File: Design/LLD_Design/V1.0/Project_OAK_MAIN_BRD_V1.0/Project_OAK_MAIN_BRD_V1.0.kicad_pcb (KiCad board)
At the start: 4 copper layers, 41.8 x 46 mm, 114 parts, among them U1 ATmega328PB-MU, U2 RV-8263-C7-32.768KHZ-20PPM-TA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, U3 BMA400, U4 DRV2605LYZF

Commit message: Final files prior to DFM check
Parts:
- added G***: LOGO, AI_logo:Project_OAK_V1.0_logo, F.Cu at (73.1, 99.6)
- added G***: LOGO, AI_logo:Project_OAK_V1.0_logo, F.Cu at (70.9, 100.0)
- added G***: LOGO, AI_logo:AI_logo_v1, F.Cu at (70.5, 90.8)
- moved TP7 3.82 mm to (71.7, 96.1)
- moved TP6 2.93 mm to (69.2, 96.1)
- moved TP11 2.73 mm to (67.3, 92.1)
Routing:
- net /PB7: track 4.90 -> 2.03 mm
- net /PB6: track 2.23 -> 4.99 mm
- net /LGT_ON_BTN: track 25.0 -> 27.5 mm
- net /PE1: track 25.2 -> 26.7 mm
- net /UP_BTN: track 27.3 -> 28.7 mm
- net /SNS_SCL: track 27.4 -> 28.4 mm
- net /RTC_CLKO: track 3.71 -> 4.53 mm
- net GND: track 76.8 -> 76.2 mm, vias 75 -> 74
- net /PE2: track 17.9 -> 17.7 mm, vias 2 -> 3

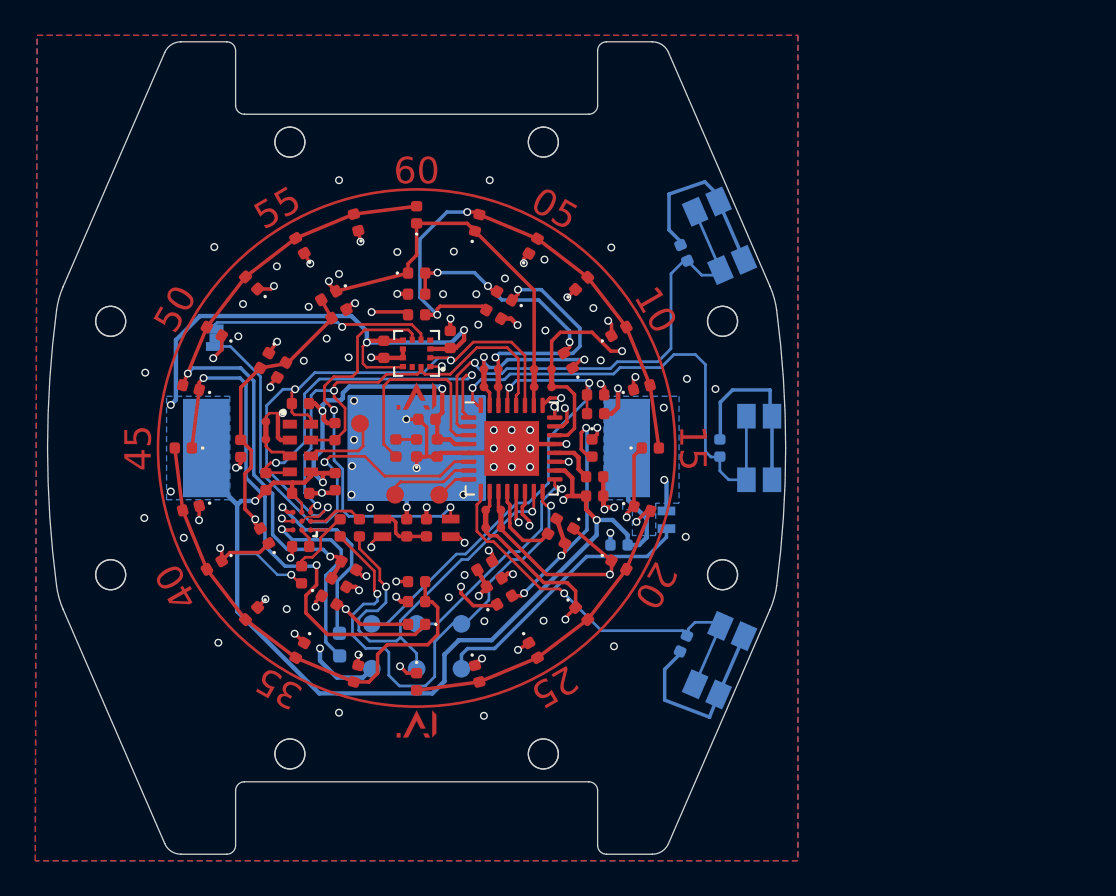
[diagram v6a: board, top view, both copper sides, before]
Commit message: updated PCB based on JLCPCB DFM comments and generated final files
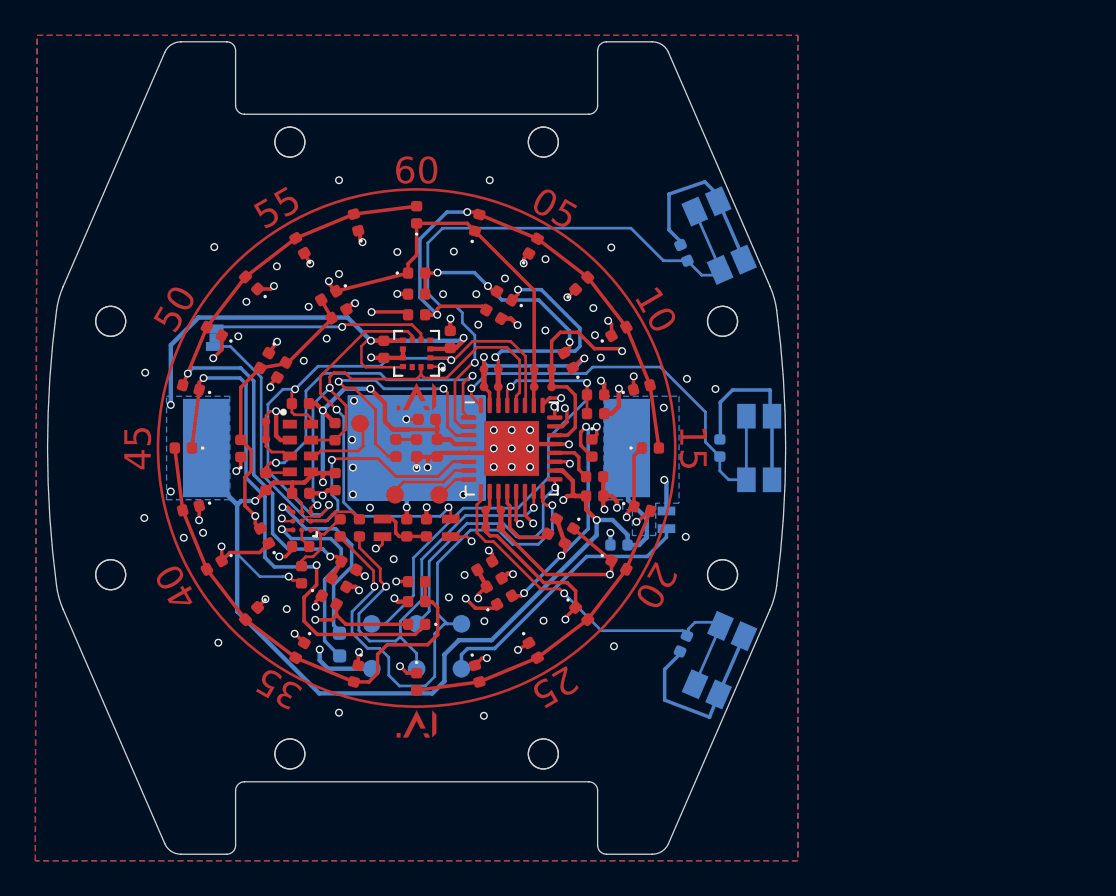
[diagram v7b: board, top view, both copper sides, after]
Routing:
- net /UP_BTN: track 28.7 -> 35.4 mm
- net /MON_LED: track 12.1 -> 15.9 mm, vias 0 -> 2
- net /ICSP_MISO: track 28.5 -> 32.0 mm
- net +3V0: track 137.8 -> 134.8 mm
- net /LGT_ON_BTN: track 27.5 -> 25.0 mm
- net /ICSP_SCK: track 13.2 -> 14.8 mm
- net GND: track 76.2 -> 74.9 mm, vias 74 -> 77
- net /ACC_INT2: track 22.4 -> 21.5 mm
- net /R5: track 88.9 -> 89.8 mm
- net /R2: track 65.9 -> 66.8 mm
- net /ICSP_MOSI: track 24.2 -> 25.1 mm
- net /MCU_RSTn: track 27.5 -> 28.4 mm
- net /PE1: track 26.7 -> 26.0 mm
- net /LED MATRIX/C2_T: track 29.5 -> 30.1 mm
- net /R1: track 51.4 -> 52.0 mm
